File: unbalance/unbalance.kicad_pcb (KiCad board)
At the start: 2 copper layers, 16 parts, among them P1 power, P2 bal, P3 CONN_01X02, P4 CONN_01X02, U1 INA134

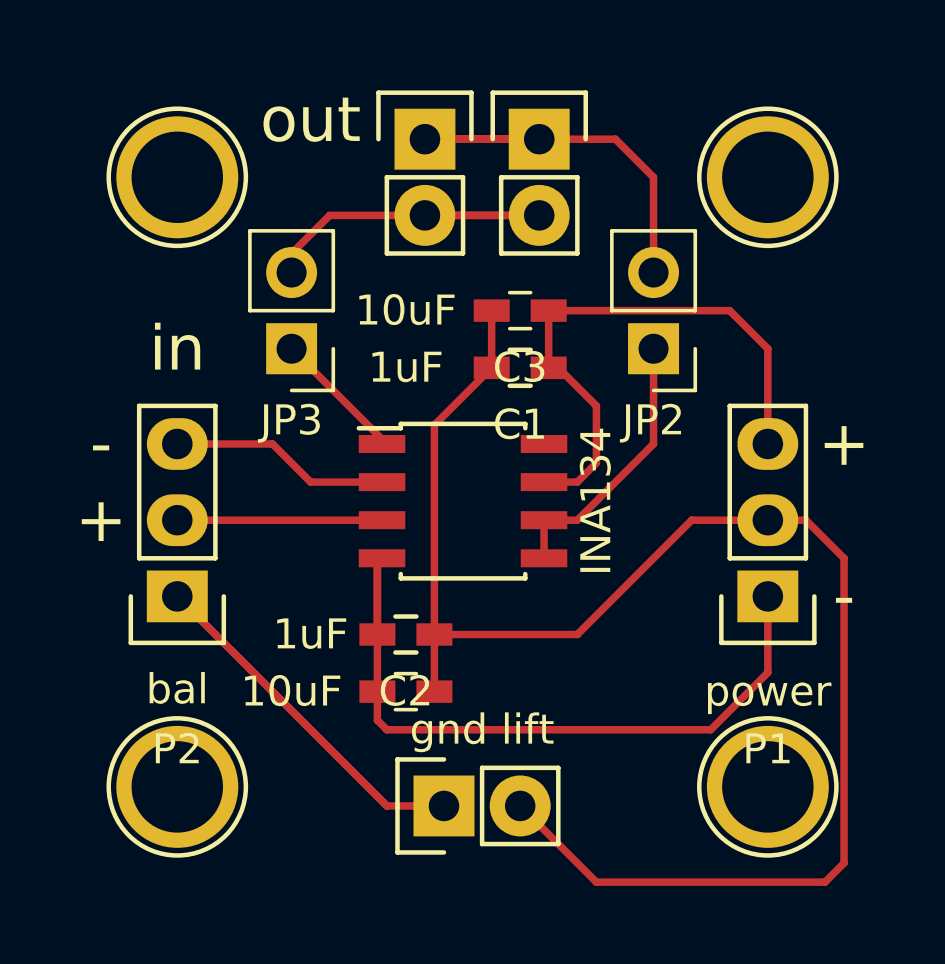
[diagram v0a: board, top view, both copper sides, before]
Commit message: Consistent quadratic soldermask is plus
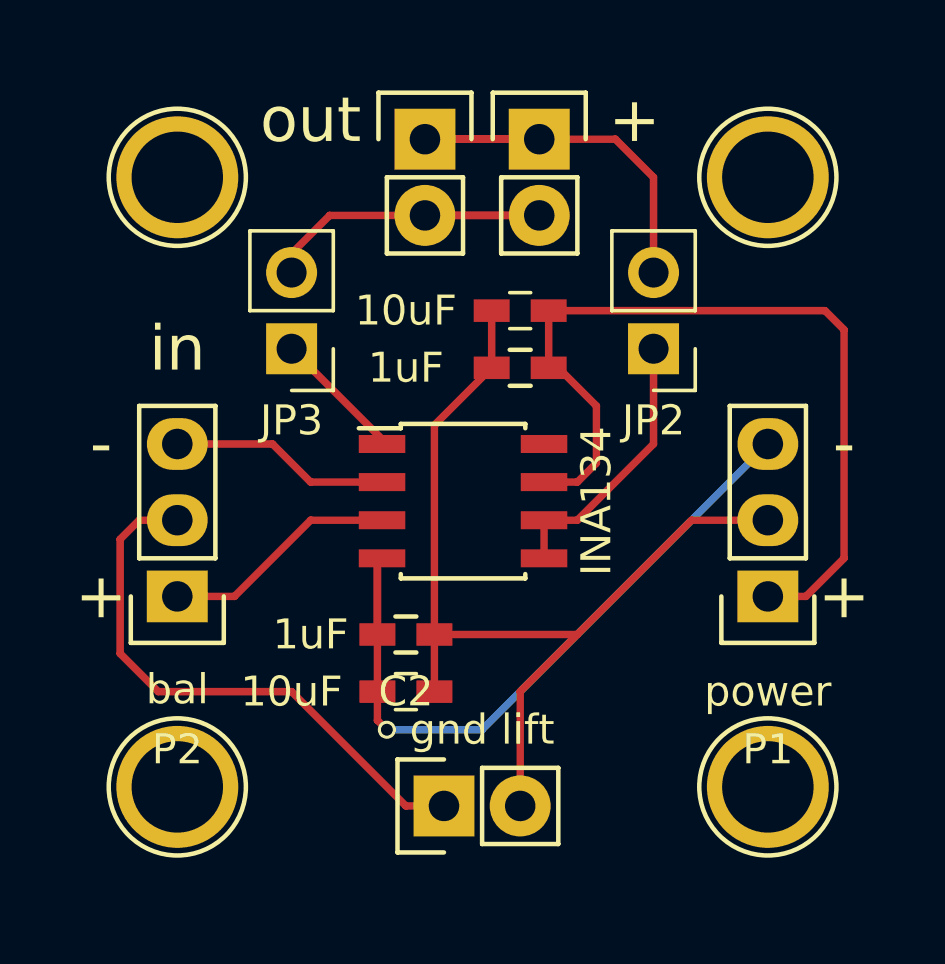
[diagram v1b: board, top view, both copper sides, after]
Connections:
- P1 pad 1: -15V -> +15V
- P1 pad 3: +15V -> -15V
- P2 pad 1: Net-(JP1-Pad1) -> Net-(P2-Pad1)
- P2 pad 2: Net-(P2-Pad2) -> Net-(JP1-Pad1)
- U1 pad 3: Net-(P2-Pad2) -> Net-(P2-Pad1)
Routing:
- net GNDA: track 51.8 -> 33.0 mm
- net +15V: track 18.9 -> 28.7 mm
- net Net-(P2-Pad1): track 0.00 -> 7.88 mm
- net Net-(P2-Pad2): track 6.82 -> 0.00 mm
- net Net-(JP1-Pad1): track 21.7 -> 18.9 mm
- net -15V: track 24.5 -> 25.2 mm, vias 0 -> 1

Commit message: ADC
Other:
- board outline added: 27.3 x 27.9 mm

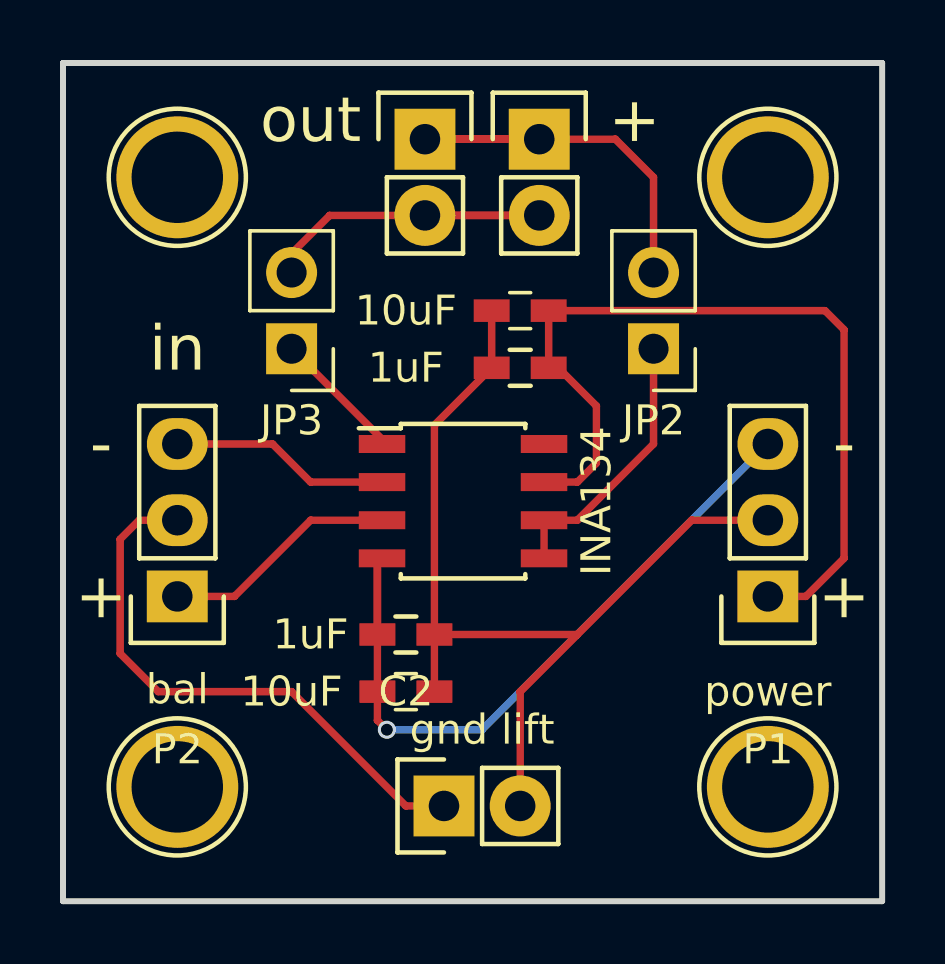
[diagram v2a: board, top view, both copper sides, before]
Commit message: Combine libraries
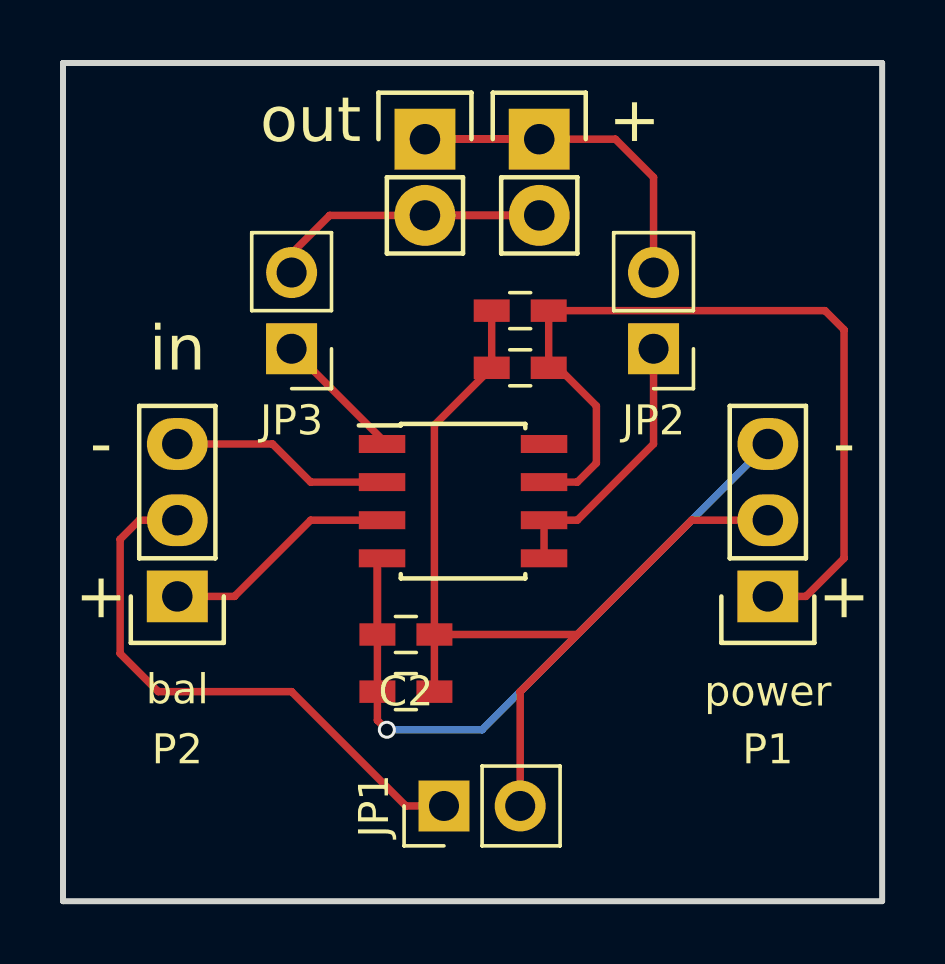
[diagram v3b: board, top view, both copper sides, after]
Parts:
- removed ? (x3): , Connect:1pin
- removed ?: 1pin, Connect:1pin
- JP1: footprint Pin_Headers:Pin_Header_Straight_1x02 -> Pin_Headers:Pin_Header_Straight_1x02_Pitch2.54mm
